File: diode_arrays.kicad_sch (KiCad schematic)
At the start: 13 parts

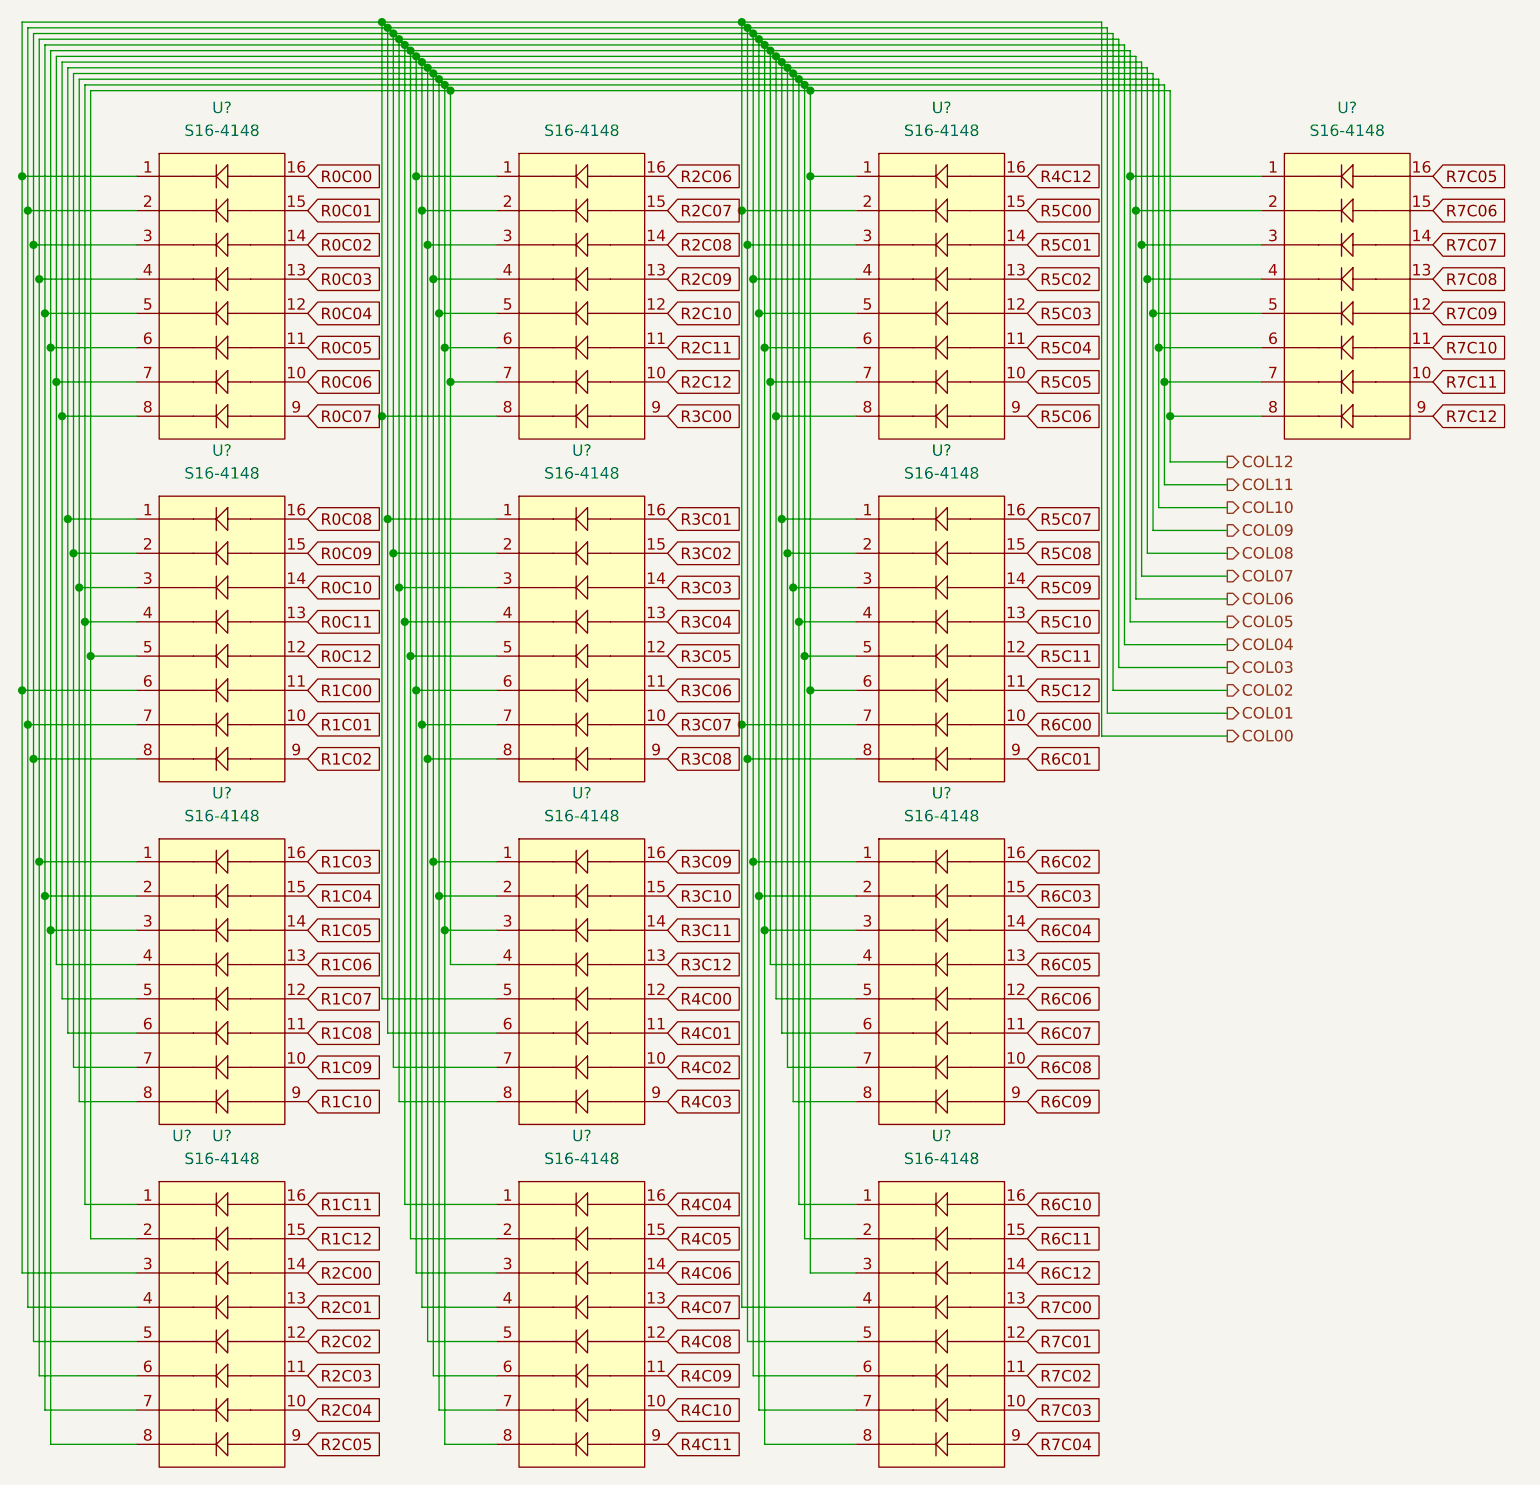
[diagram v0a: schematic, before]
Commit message: Add RGB LEDs, assign footpritns, begin placement
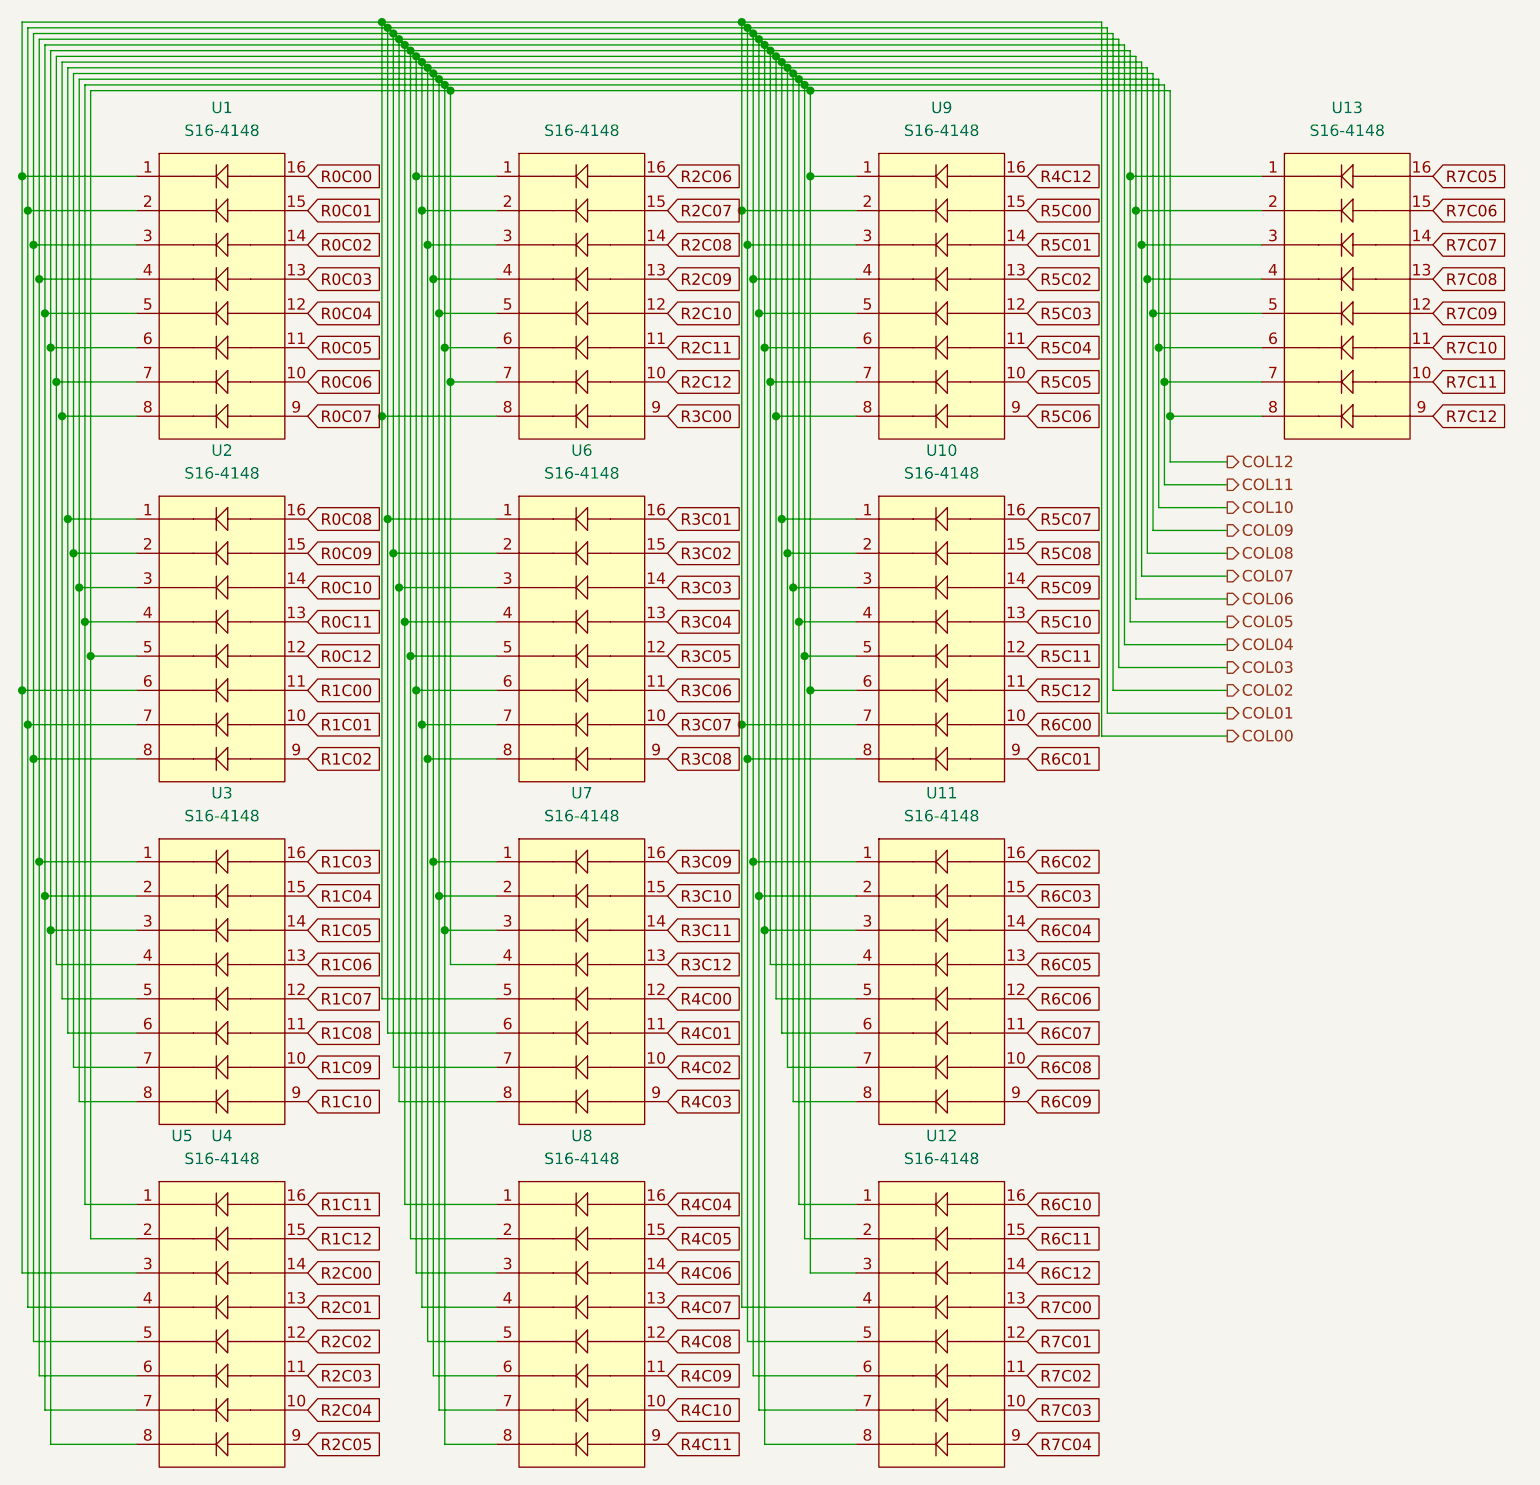
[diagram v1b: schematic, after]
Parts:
- U1, U10, U11, U12, U13, U2, U3, U4, U5, U6, U7, U8, U9: renamed from U?; footprint (none) -> Package_SO:SOIC-16_3.9x9.9mm_P1.27mm
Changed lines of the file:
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@@
   (symbol (lib_id "Arrays:S16-4148") (at 66.675 180.34 0) (unit 1)
     (in_bom yes) (on_board yes) (fields_autoplaced)
-    (property "Reference" "U?" (id 0) (at 73.66 143.51 0))
+    (property "Reference" "U4" (id 0) (at 73.66 143.51 0))
     (property "Value" "S16-4148" (id 1) (at 73.66 146.05 0))
-    (property "Footprint" "" (id 2) (at 67.945 147.32 0)
+    (property "Footprint" "Package_SO:SOIC-16_3.9x9.9mm_P1.27mm" (id 2) (at 67.945 147.32 0)
       (effects (font (size 1.27 1.27)) hide)
     )
@@
   (symbol (lib_name "S16-4148_7") (lib_id "Arrays:S16-4148") (at 146.685 66.04 0) (unit 1)
     (in_bom yes) (on_board yes) (fields_autoplaced)
-    (property "Reference" "U?" (id 0) (at 153.67 29.21 0))
+    (property "Reference" "U9" (id 0) (at 153.67 29.21 0))
     (property "Value" "S16-4148" (id 1) (at 153.67 31.75 0))
-    (property "Footprint" "" (id 2) (at 147.955 33.02 0)
+    (property "Footprint" "Package_SO:SOIC-16_3.9x9.9mm_P1.27mm" (id 2) (at 147.955 33.02 0)
       (effects (font (size 1.27 1.27)) hide)
     )
@@
     (pin "9")
   )
-  (symbol (lib_name "S16-4148_9") (lib_id "Arrays:S16-4148") (at 66.675 66.04 0) (unit 1)
-    (in_bom yes) (on_board yes) (fields_autoplaced)
-    (property "Reference" "U?" (id 0) (at 73.66 29.21 0))
+  (symbol (lib_id "Arrays:S16-4148") (at 66.675 66.04 0) (unit 1)
+    (in_bom yes) (on_board yes) (fields_autoplaced)
+    (property "Reference" "U1" (id 0) (at 73.66 29.21 0))
     (property "Value" "S16-4148" (id 1) (at 73.66 31.75 0))
-    (property "Footprint" "" (id 2) (at 67.945 33.02 0)
+    (property "Footprint" "Package_SO:SOIC-16_3.9x9.9mm_P1.27mm" (id 2) (at 67.945 33.02 0)
       (effects (font (size 1.27 1.27)) hide)
     )
@@
   (symbol (lib_name "S16-4148_2") (lib_id "Arrays:S16-4148") (at 146.685 180.34 0) (unit 1)
     (in_bom yes) (on_board yes) (fields_autoplaced)
-    (property "Reference" "U?" (id 0) (at 153.67 143.51 0))
+    (property "Reference" "U12" (id 0) (at 153.67 143.51 0))
     (property "Value" "S16-4148" (id 1) (at 153.67 146.05 0))
-    (property "Footprint" "" (id 2) (at 147.955 147.32 0)
+    (property "Footprint" "Package_SO:SOIC-16_3.9x9.9mm_P1.27mm" (id 2) (at 147.955 147.32 0)
       (effects (font (size 1.27 1.27)) hide)
     )
@@
   (symbol (lib_name "S16-4148_11") (lib_id "Arrays:S16-4148") (at 106.68 104.14 0) (unit 1)
     (in_bom yes) (on_board yes) (fields_autoplaced)
-    (property "Reference" "U?" (id 0) (at 113.665 67.31 0))
+    (property "Reference" "U6" (id 0) (at 113.665 67.31 0))
     (property "Value" "S16-4148" (id 1) (at 113.665 69.85 0))
-    (property "Footprint" "" (id 2) (at 107.95 71.12 0)
+    (property "Footprint" "Package_SO:SOIC-16_3.9x9.9mm_P1.27mm" (id 2) (at 107.95 71.12 0)
       (effects (font (size 1.27 1.27)) hide)
     )
@@
     (pin "9")
   )
-  (symbol (lib_name "S16-4148_8") (lib_id "Arrays:S16-4148") (at 106.68 66.04 0) (unit 1)
+  (symbol (lib_id "Arrays:S16-4148") (at 106.68 66.04 0) (unit 1)
     (in_bom yes) (on_board yes)
-    (property "Reference" "U?" (id 0) (at 69.215 143.51 0))
+    (property "Reference" "U5" (id 0) (at 69.215 143.51 0))
     (property "Value" "S16-4148" (id 1) (at 113.665 31.75 0))
-    (property "Footprint" "" (id 2) (at 107.95 33.02 0)
+    (property "Footprint" "Package_SO:SOIC-16_3.9x9.9mm_P1.27mm" (id 2) (at 107.95 33.02 0)
       (effects (font (size 1.27 1.27)) hide)
     )
@@
     (pin "9")
   )
-  (symbol (lib_name "S16-4148_12") (lib_id "Arrays:S16-4148") (at 66.675 104.14 0) (unit 1)
-    (in_bom yes) (on_board yes) (fields_autoplaced)
-    (property "Reference" "U?" (id 0) (at 73.66 67.31 0))
+  (symbol (lib_id "Arrays:S16-4148") (at 66.675 104.14 0) (unit 1)
+    (in_bom yes) (on_board yes) (fields_autoplaced)
+    (property "Reference" "U2" (id 0) (at 73.66 67.31 0))
     (property "Value" "S16-4148" (id 1) (at 73.66 69.85 0))
-    (property "Footprint" "" (id 2) (at 67.945 71.12 0)
+    (property "Footprint" "Package_SO:SOIC-16_3.9x9.9mm_P1.27mm" (id 2) (at 67.945 71.12 0)
       (effects (font (size 1.27 1.27)) hide)
     )
@@
   (symbol (lib_name "S16-4148_1") (lib_id "Arrays:S16-4148") (at 146.685 104.14 0) (unit 1)
     (in_bom yes) (on_board yes) (fields_autoplaced)
-    (property "Reference" "U?" (id 0) (at 153.67 67.31 0))
+    (property "Reference" "U10" (id 0) (at 153.67 67.31 0))
     (property "Value" "S16-4148" (id 1) (at 153.67 69.85 0))
-    (property "Footprint" "" (id 2) (at 147.955 71.12 0)
+    (property "Footprint" "Package_SO:SOIC-16_3.9x9.9mm_P1.27mm" (id 2) (at 147.955 71.12 0)
       (effects (font (size 1.27 1.27)) hide)
     )
@@
   (symbol (lib_name "S16-4148_4") (lib_id "Arrays:S16-4148") (at 191.77 66.04 0) (unit 1)
     (in_bom yes) (on_board yes) (fields_autoplaced)
-    (property "Reference" "U?" (id 0) (at 198.755 29.21 0))
+    (property "Reference" "U13" (id 0) (at 198.755 29.21 0))
     (property "Value" "S16-4148" (id 1) (at 198.755 31.75 0))
-    (property "Footprint" "" (id 2) (at 193.04 33.02 0)
+    (property "Footprint" "Package_SO:SOIC-16_3.9x9.9mm_P1.27mm" (id 2) (at 193.04 33.02 0)
       (effects (font (size 1.27 1.27)) hide)
     )
@@
     (pin "9")
   )
-  (symbol (lib_name "S16-4148_5") (lib_id "Arrays:S16-4148") (at 106.68 142.24 0) (unit 1)
-    (in_bom yes) (on_board yes) (fields_autoplaced)
-    (property "Reference" "U?" (id 0) (at 113.665 105.41 0))
+  (symbol (lib_id "Arrays:S16-4148") (at 106.68 142.24 0) (unit 1)
+    (in_bom yes) (on_board yes) (fields_autoplaced)
+    (property "Reference" "U7" (id 0) (at 113.665 105.41 0))
     (property "Value" "S16-4148" (id 1) (at 113.665 107.95 0))
-    (property "Footprint" "" (id 2) (at 107.95 109.22 0)
+    (property "Footprint" "Package_SO:SOIC-16_3.9x9.9mm_P1.27mm" (id 2) (at 107.95 109.22 0)
       (effects (font (size 1.27 1.27)) hide)
     )
@@
   (symbol (lib_name "S16-4148_6") (lib_id "Arrays:S16-4148") (at 106.68 180.34 0) (unit 1)
     (in_bom yes) (on_board yes) (fields_autoplaced)
-    (property "Reference" "U?" (id 0) (at 113.665 143.51 0))
+    (property "Reference" "U8" (id 0) (at 113.665 143.51 0))
     (property "Value" "S16-4148" (id 1) (at 113.665 146.05 0))
-    (property "Footprint" "" (id 2) (at 107.95 147.32 0)
+    (property "Footprint" "Package_SO:SOIC-16_3.9x9.9mm_P1.27mm" (id 2) (at 107.95 147.32 0)
       (effects (font (size 1.27 1.27)) hide)
     )
@@
   (symbol (lib_name "S16-4148_3") (lib_id "Arrays:S16-4148") (at 146.685 142.24 0) (unit 1)
     (in_bom yes) (on_board yes) (fields_autoplaced)
-    (property "Reference" "U?" (id 0) (at 153.67 105.41 0))
+    (property "Reference" "U11" (id 0) (at 153.67 105.41 0))
     (property "Value" "S16-4148" (id 1) (at 153.67 107.95 0))
-    (property "Footprint" "" (id 2) (at 147.955 109.22 0)
+    (property "Footprint" "Package_SO:SOIC-16_3.9x9.9mm_P1.27mm" (id 2) (at 147.955 109.22 0)
       (effects (font (size 1.27 1.27)) hide)
     )
@@
     (pin "9")
   )
-  (symbol (lib_name "S16-4148_10") (lib_id "Arrays:S16-4148") (at 66.675 142.24 0) (unit 1)
-    (in_bom yes) (on_board yes) (fields_autoplaced)
-    (property "Reference" "U?" (id 0) (at 73.66 105.41 0))
+  (symbol (lib_id "Arrays:S16-4148") (at 66.675 142.24 0) (unit 1)
+    (in_bom yes) (on_board yes) (fields_autoplaced)
+    (property "Reference" "U3" (id 0) (at 73.66 105.41 0))
     (property "Value" "S16-4148" (id 1) (at 73.66 107.95 0))
-    (property "Footprint" "" (id 2) (at 67.945 109.22 0)
-      (effects (font (size 1.27 1.27)) hide)
-    )
+    (property "Footprint" "Package_SO:SOIC-16_3.9x9.9mm_P1.27mm" (id 2) (at 67.945 109.22 0)
+      (effects (font (size 1.27 1.27)) hide)
+    )
